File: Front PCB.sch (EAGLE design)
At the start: 10 parts

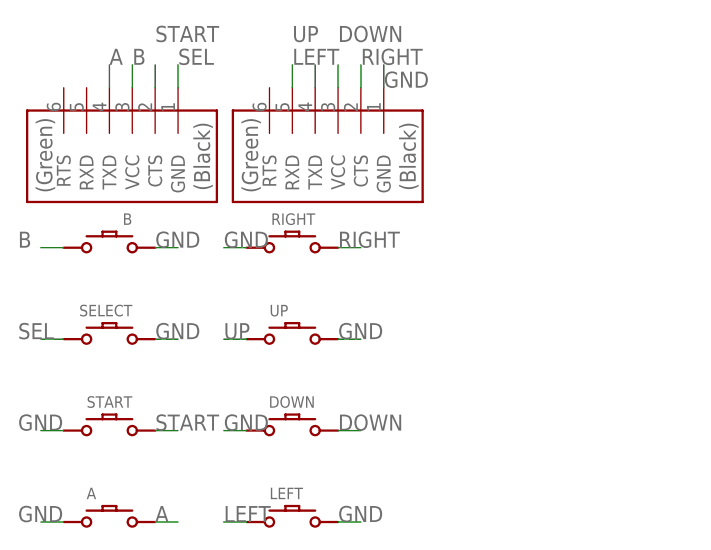
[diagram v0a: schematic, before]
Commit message: Redesign board to use through-hole pins
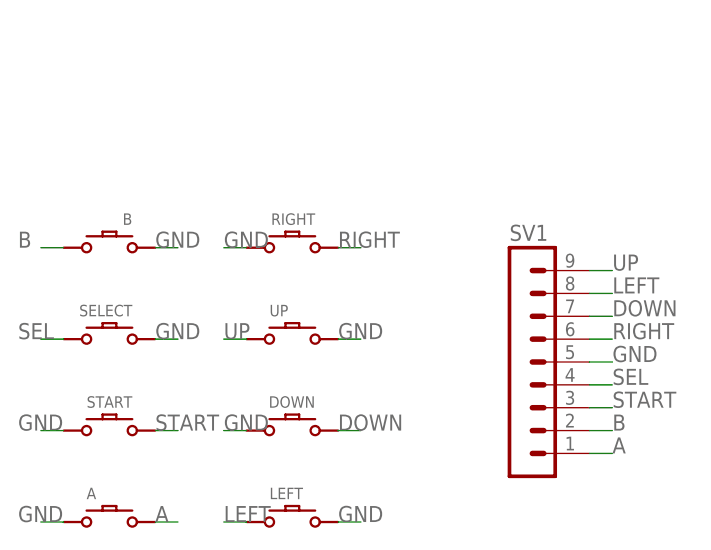
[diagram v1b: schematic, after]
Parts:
- removed U$1, U$2: FTDI-SMD-HEADER, fab:FTDI-SMD-HEADER
- added SV1: (no value), con-lstb:MA09-1
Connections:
- net A: now also SV1.1; no longer U$1.TXD
- net B: now also SV1.2; no longer U$1.VCC
- net DOWN: now also SV1.7; no longer U$2.VCC
- net GND: now also SV1.5; no longer U$2.GND
- net LEFT: now also SV1.8; no longer U$2.TXD
- net RIGHT: now also SV1.6; no longer U$2.CTS
- net SEL: now also SV1.4; no longer U$1.GND
- net START: now also SV1.3; no longer U$1.CTS
- net UP: now also SV1.9; no longer U$2.RXD
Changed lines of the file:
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@@
 <part name="DOWN" library="Game Boy" deviceset="DMG-BTN" device="REGULAR" value="DMG-BTN"/>
 <part name="START" library="Game Boy" deviceset="DMG-BTN" device="START" value="DMG-BTN"/>
-<part name="U$1" library="fab" deviceset="FTDI-SMD-HEADER" device=""/>
-<part name="U$2" library="fab" deviceset="FTDI-SMD-HEADER" device=""/>
+<part name="SV1" library="con-lstb" deviceset="MA09-1" device=""/>
 </parts>
 <sheets>
@@
 <instance part="DOWN" gate="G$1" x="317.5" y="35.56" rot="MR0"/>
 <instance part="START" gate="G$1" x="297.18" y="35.56" rot="MR0"/>
-<instance part="U$1" gate="G$1" x="292.1" y="73.66" rot="R270"/>
-<instance part="U$2" gate="G$1" x="314.96" y="73.66" rot="R270"/>
+<instance part="SV1" gate="1" x="342.9" y="43.18"/>
 </instances>
 <busses>
@@
 </segment>
 <segment>
-<pinref part="U$1" gate="G$1" pin="VCC"/>
-<wire x1="299.72" y1="76.2" x2="299.72" y2="73.66" width="0.1524" layer="91"/>
-<label x="299.72" y="76.2" size="1.778" layer="95"/>
+<pinref part="SV1" gate="1" pin="2"/>
+<wire x1="353.06" y1="35.56" x2="350.52" y2="35.56" width="0.1524" layer="91"/>
+<label x="353.06" y="35.56" size="1.778" layer="95"/>
 </segment>
 </net>
@@
 </segment>
 <segment>
-<pinref part="U$1" gate="G$1" pin="GND"/>
-<wire x1="304.8" y1="76.2" x2="304.8" y2="73.66" width="0.1524" layer="91"/>
-<label x="304.8" y="76.2" size="1.778" layer="95"/>
+<pinref part="SV1" gate="1" pin="4"/>
+<wire x1="353.06" y1="40.64" x2="350.52" y2="40.64" width="0.1524" layer="91"/>
+<label x="353.06" y="40.64" size="1.778" layer="95"/>
 </segment>
 </net>
@@
 </segment>
 <segment>
-<pinref part="U$1" gate="G$1" pin="CTS"/>
-<wire x1="302.26" y1="76.2" x2="302.26" y2="73.66" width="0.1524" layer="91"/>
-<label x="302.26" y="78.74" size="1.778" layer="95"/>
+<pinref part="SV1" gate="1" pin="3"/>
+<wire x1="353.06" y1="38.1" x2="350.52" y2="38.1" width="0.1524" layer="91"/>
+<label x="353.06" y="38.1" size="1.778" layer="95"/>
 </segment>
 </net>
@@
 </segment>
 <segment>
-<pinref part="U$1" gate="G$1" pin="TXD"/>
-<wire x1="297.18" y1="76.2" x2="297.18" y2="73.66" width="0.1524" layer="91"/>
-<label x="297.18" y="76.2" size="1.778" layer="95"/>
+<pinref part="SV1" gate="1" pin="1"/>
+<wire x1="353.06" y1="33.02" x2="350.52" y2="33.02" width="0.1524" layer="91"/>
+<label x="353.06" y="33.02" size="1.778" layer="95"/>
 </segment>
 </net>
@@
 </segment>
 <segment>
-<pinref part="U$2" gate="G$1" pin="TXD"/>
-<wire x1="320.04" y1="76.2" x2="320.04" y2="73.66" width="0.1524" layer="91"/>
-<label x="317.5" y="76.2" size="1.778" layer="95"/>
+<pinref part="SV1" gate="1" pin="8"/>
+<wire x1="353.06" y1="50.8" x2="350.52" y2="50.8" width="0.1524" layer="91"/>
+<label x="353.06" y="50.8" size="1.778" layer="95"/>
 </segment>
 </net>
@@
 </segment>
 <segment>
-<pinref part="U$2" gate="G$1" pin="RXD"/>
-<wire x1="317.5" y1="76.2" x2="317.5" y2="73.66" width="0.1524" layer="91"/>
-<label x="317.5" y="78.74" size="1.778" layer="95"/>
+<pinref part="SV1" gate="1" pin="9"/>
+<wire x1="353.06" y1="53.34" x2="350.52" y2="53.34" width="0.1524" layer="91"/>
+<label x="353.06" y="53.34" size="1.778" layer="95"/>
 </segment>
 </net>
@@
 </segment>
 <segment>
-<pinref part="U$2" gate="G$1" pin="VCC"/>
-<wire x1="322.58" y1="76.2" x2="322.58" y2="73.66" width="0.1524" layer="91"/>
-<label x="322.58" y="78.74" size="1.778" layer="95"/>
+<pinref part="SV1" gate="1" pin="7"/>
+<wire x1="353.06" y1="48.26" x2="350.52" y2="48.26" width="0.1524" layer="91"/>
+<label x="353.06" y="48.26" size="1.778" layer="95"/>
 </segment>
 </net>
@@
 </segment>
 <segment>
-<pinref part="U$2" gate="G$1" pin="CTS"/>
-<wire x1="325.12" y1="76.2" x2="325.12" y2="73.66" width="0.1524" layer="91"/>
-<label x="325.12" y="76.2" size="1.778" layer="95"/>
+<pinref part="SV1" gate="1" pin="6"/>
+<wire x1="353.06" y1="45.72" x2="350.52" y2="45.72" width="0.1524" layer="91"/>
+<label x="353.06" y="45.72" size="1.778" layer="95"/>
 </segment>
 </net>
@@
 <wire x1="325.12" y1="25.4" x2="322.58" y2="25.4" width="0.1524" layer="91"/>
 <label x="322.58" y="25.4" size="1.778" layer="95"/>
-</segment>
-<segment>
-<pinref part="U$2" gate="G$1" pin="GND"/>
-<wire x1="327.66" y1="76.2" x2="327.66" y2="73.66" width="0.1524" layer="91"/>
-<label x="327.66" y="73.66" size="1.778" layer="95"/>
 </segment>
 <segment>
@@
 <label x="287.02" y="25.4" size="1.778" layer="95"/>
 </segment>
+<segment>
+<pinref part="SV1" gate="1" pin="5"/>
+<wire x1="353.06" y1="43.18" x2="350.52" y2="43.18" width="0.1524" layer="91"/>
+<label x="353.06" y="43.18" size="1.778" layer="95"/>
+</segment>
 </net>
